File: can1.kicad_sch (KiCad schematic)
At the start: 7 parts, among them U1 TJA1042T-3

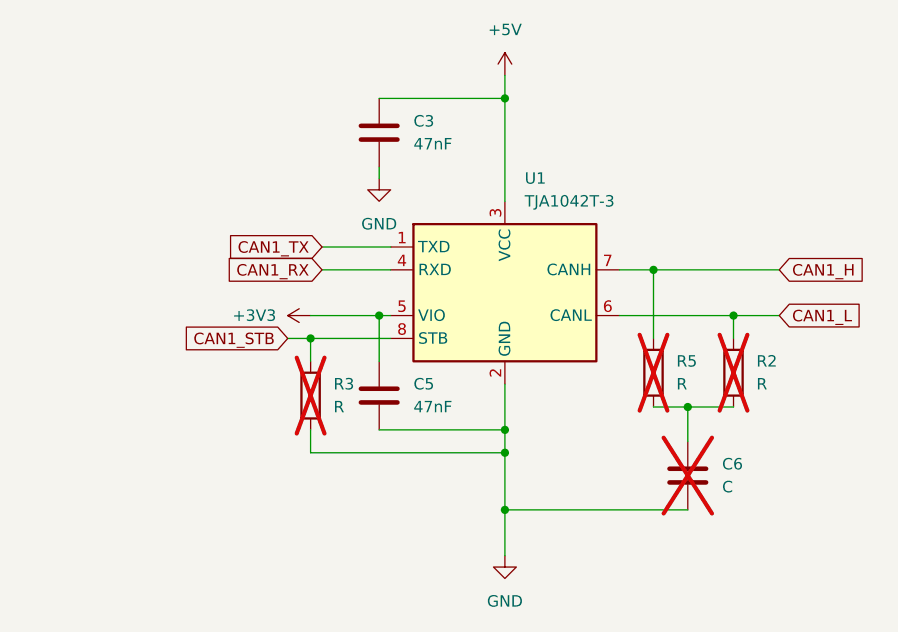
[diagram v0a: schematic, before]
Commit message: fix double numbers
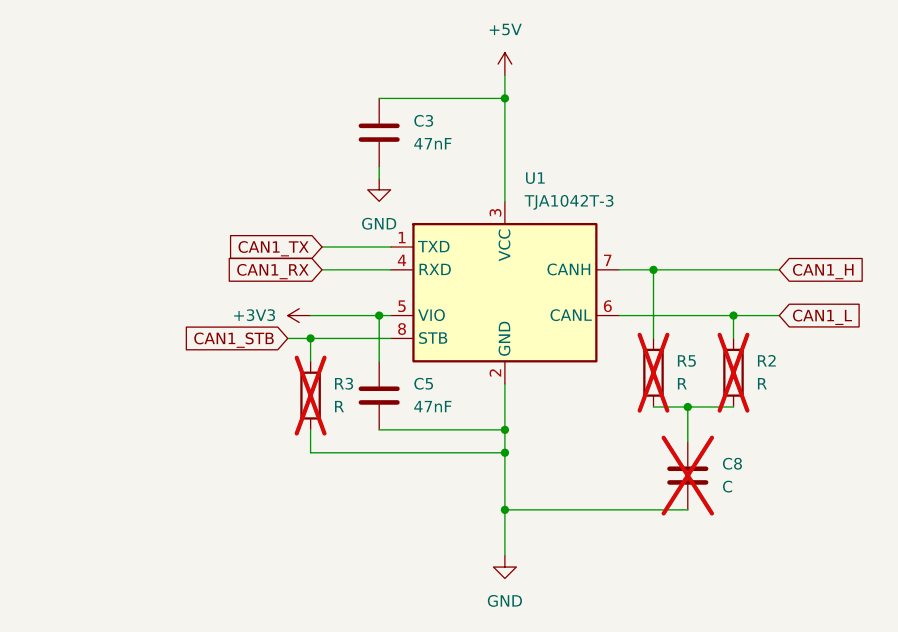
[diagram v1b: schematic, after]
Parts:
- renumbered C6 to C8
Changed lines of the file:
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@@
 		(pin "1"
+		)
+		(instances
+			(project "sample"
+				(path "/b24c09df-2e49-4fc3-a45d-ba0b1ff2d257/a1e1f3d2-08a6-4ef9-b40d-891f90ca343c"
+					(reference "C5")
+					(unit 1)
+				)
+			)
 		)
 	)
@@
 		(pin "1"
 		)
+		(instances
+			(project "sample"
+				(path "/b24c09df-2e49-4fc3-a45d-ba0b1ff2d257/a1e1f3d2-08a6-4ef9-b40d-891f90ca343c"
+					(reference "R5")
+					(unit 1)
+				)
+			)
+		)
 	)
 	(symbol
@@
 		(pin "1"
 		)
+		(instances
+			(project "sample"
+				(path "/b24c09df-2e49-4fc3-a45d-ba0b1ff2d257/a1e1f3d2-08a6-4ef9-b40d-891f90ca343c"
+					(reference "#PWR018")
+					(unit 1)
+				)
+			)
+		)
 	)
 	(symbol
@@
 		(dnp yes)
 		(fields_autoplaced yes)
-		(property "Reference" "C6"
+		(property "Reference" "C8"
 			(at 149.86 101.5999 0)
 			(effects
@@
 		(pin "1"
 		)
-	)
+		(instances
+			(project "sample"
+				(path "/b24c09df-2e49-4fc3-a45d-ba0b1ff2d257/a1e1f3d2-08a6-4ef9-b40d-891f90ca343c"
+					(reference "C8")
+					(unit 1)
+				)
+			)
+		)
+	)

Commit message: add CAN STB pins
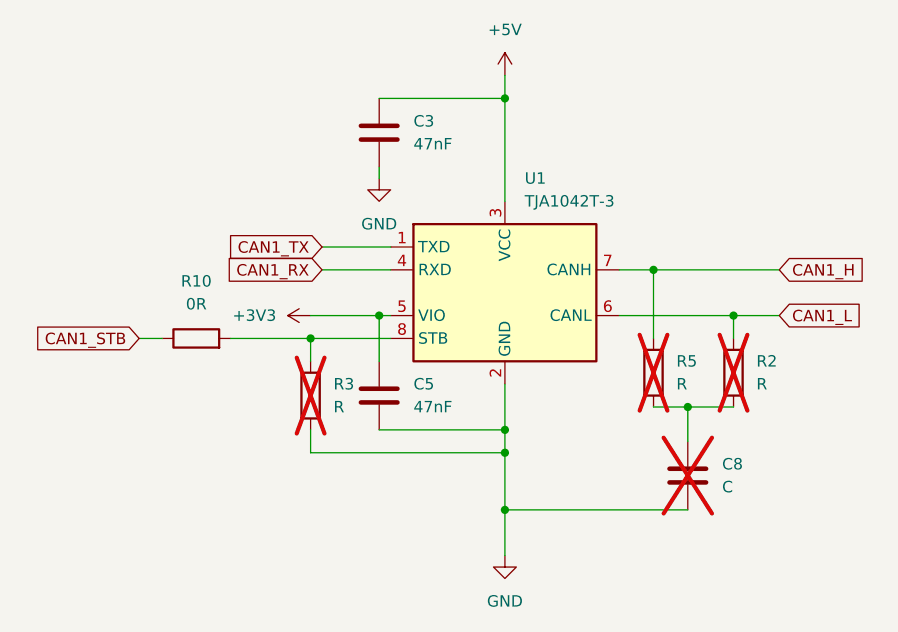
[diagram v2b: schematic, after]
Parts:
- added R10: 0R, Resistor_SMD:R_1206_3216Metric_Pad1.30x1.75mm_HandSolder, symbol Device:R
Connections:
- net CAN1_STB: now also R10.1; no longer R3.1, U1.8 (STB)
- new net: R10.2, R3.1, U1.8 (STB)
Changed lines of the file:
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@@
+	)
+	(junction
+		(at 125.73 106.68)
+		(diameter 0)
+		(color 0 0 0 0)
+	)
+	(junction
+		(at 151.13 85.09)
+		(diameter 0)
+		(color 0 0 0 0)
+	)
+	(junction
+		(at 125.73 100.33)
+		(diameter 0)
+		(color 0 0 0 0)
+	)
+	(junction
+		(at 142.24 80.01)
+		(diameter 0)
+		(color 0 0 0 0)
+	)
+	(junction
+		(at 111.76 85.09)
+		(diameter 0)
+		(color 0 0 0 0)
+	)
+	(junction
+		(at 125.73 97.79)
+		(diameter 0)
+		(color 0 0 0 0)
 	)
 	(junction
@@
 	)
 	(junction
-		(at 125.73 106.68)
-		(diameter 0)
-		(color 0 0 0 0)
-	)
-	(junction
-		(at 151.13 85.09)
-		(diameter 0)
-		(color 0 0 0 0)
-	)
-	(junction
-		(at 125.73 100.33)
-		(diameter 0)
-		(color 0 0 0 0)
-	)
-	(junction
-		(at 142.24 80.01)
-		(diameter 0)
-		(color 0 0 0 0)
-	)
-	(junction
-		(at 111.76 85.09)
-		(diameter 0)
-		(color 0 0 0 0)
-	)
-	(junction
-		(at 125.73 97.79)
-		(diameter 0)
-		(color 0 0 0 0)
-	)
-	(junction
 		(at 146.05 95.25)
 		(diameter 0)
@@
 	(wire
 		(pts
+			(xy 95.25 87.63) (xy 104.14 87.63)
+		)
+		(stroke
+			(width 0)
+			(type default)
+		)
+	)
+	(wire
+		(pts
 			(xy 125.73 92.71) (xy 125.73 97.79)
 		)
@@
 	(wire
 		(pts
-			(xy 101.6 87.63) (xy 104.14 87.63)
-		)
-		(stroke
-			(width 0)
-			(type default)
-		)
-	)
-	(wire
-		(pts
 			(xy 104.14 97.79) (xy 104.14 100.33)
 		)
@@
 		(pts
 			(xy 151.13 85.09) (xy 156.21 85.09)
+		)
+		(stroke
+			(width 0)
+			(type default)
+		)
+	)
+	(wire
+		(pts
+			(xy 85.09 87.63) (xy 87.63 87.63)
 		)
 		(stroke
@@
 	(global_label "CAN1_STB"
 		(shape input)
-		(at 101.6 87.63 180)
+		(at 85.09 87.63 180)
 		(fields_autoplaced yes)
 		(effects
@@
 		)
 		(property "Intersheetrefs" "${INTERSHEET_REFS}"
-			(at 89.3015 87.63 0)
+			(at 72.7915 87.63 0)
 			(effects
 				(font
@@
 					(unit 1)
 				)
+			)
+		)
+	)
+	(symbol
+		(lib_id "Device:R")
+		(at 91.44 87.63 90)
+		(unit 1)
+		(exclude_from_sim no)
+		(in_bom yes)
+		(on_board yes)
+		(dnp no)
+		(fields_autoplaced yes)
+		(property "Reference" "R10"
+			(at 91.44 81.28 90)
+			(effects
+				(font
+					(size 1.27 1.27)
+				)
+			)
+		)
+		(property "Value" "0R"
+			(at 91.44 83.82 90)
+			(effects
+				(font
+					(size 1.27 1.27)
+				)
+			)
+		)
+		(property "Footprint" "Resistor_SMD:R_1206_3216Metric_Pad1.30x1.75mm_HandSolder"
+			(at 91.44 89.408 90)
+			(effects
+				(font
+					(size 1.27 1.27)
+				)
+				(hide yes)
+			)
+		)
+		(property "Datasheet" "~"
+			(at 91.44 87.63 0)
+			(effects
+				(font
+					(size 1.27 1.27)
+				)
+				(hide yes)
+			)
+		)
+		(property "Description" "Resistor"
+			(at 91.44 87.63 0)
+			(effects
+				(font
+					(size 1.27 1.27)
+				)
+				(hide yes)
+			)
+		)
+		(pin "2"
+		)
+		(pin "1"
+		)
+		(instances
+			(project "sample"
+				(path "/b24c09df-2e49-4fc3-a45d-ba0b1ff2d257/a1e1f3d2-08a6-4ef9-b40d-891f90ca343c"
+					(reference "R10")
+					(unit 1)
+				)
